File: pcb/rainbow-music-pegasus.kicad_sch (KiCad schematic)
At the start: 113 parts, among them J1 USB_B_Micro, J2 Conn_02x03_Odd_Even, J3 B2B-PH-K-S, Q1 DMG3415U, SW1 SW_SPDT, SW2 EVQQ2, U1 ESP32-C3-MINI-1, U2 OPA2322, U3 TLV75533PDBV, U4 MCP73831-2-OT, U5 MCP41050

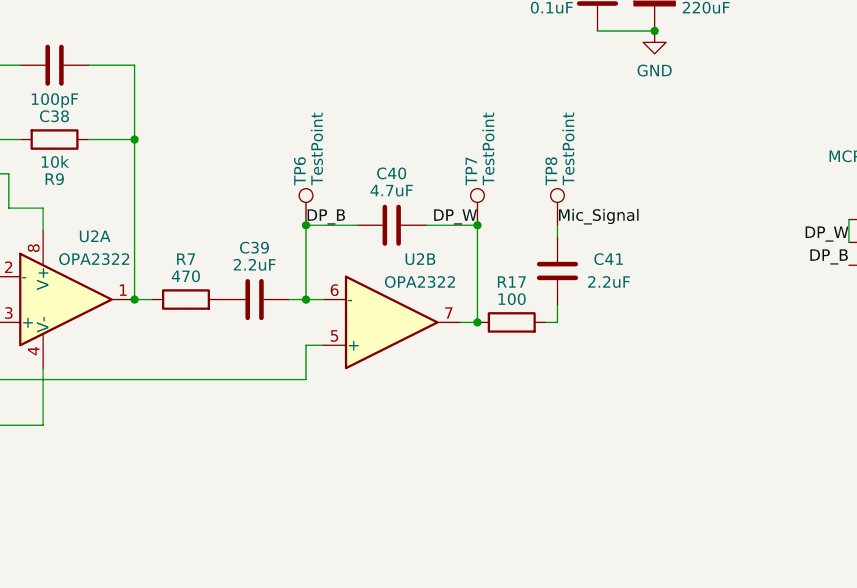
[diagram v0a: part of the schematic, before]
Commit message: Minor changes to the PCB and BOM to better support the digipot and signal
* Remove C40 (which was shunting the MCP41050 PB0 & PB0, reducing effectiveness)
* Raise R7 from 470 to 2.2k
* Raise R17 from 100 to 330
* Change C41 to a 0.1uF shunt cap to GND placed close to GPIO4

The R7 is raised 2.2k so the digipot wiper current stays within its +/-1
mA rating even if the first stage swings rail to rail, and so loud music
sits mid-range on the wiper where steps are finer (maximum stage-2 gain
is now ~23). With C39 (2.2uF) this also lowers the high-pass corner from
~154 Hz to ~33 Hz, letting bass through.

The ADC now sees U2B's 1.65 V output directly, as the firmware expects,
and R17/C41 form a ~4.8 kHz anti-aliasing filter and a charge reservoir
for ADC sampling.
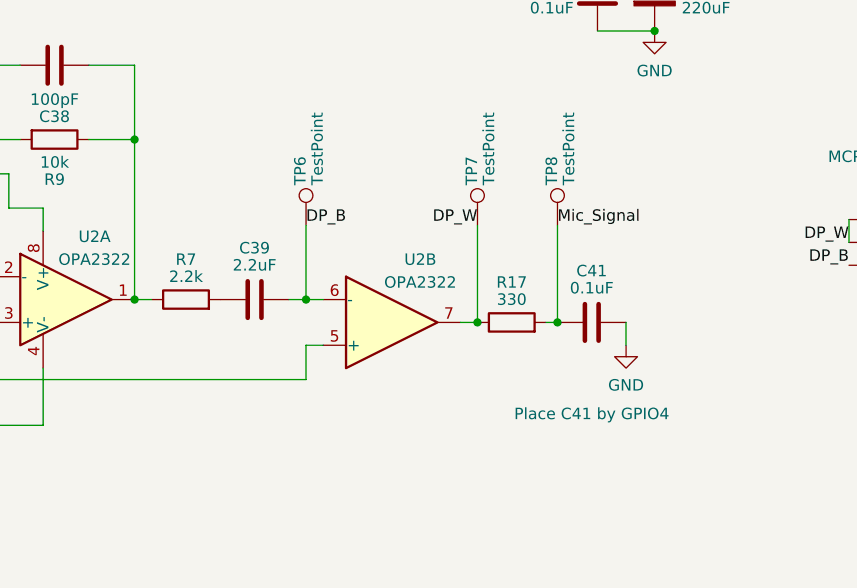
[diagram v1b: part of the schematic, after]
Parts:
- removed C40: 4.7uF, Capacitor_SMD:C_0805_2012Metric, symbol Device:C
- C41: value 2.2uF -> 0.1uF; footprint Capacitor_SMD:C_0805_2012Metric -> Capacitor_SMD:C_0603_1608Metric
- R17: value 100 -> 330
- R7: value 470 -> 2.2k; footprint Resistor_SMD:R_0603_1608Metric -> Resistor_SMD:R_0805_2012Metric
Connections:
- net GND: now also C41.2
- net Mic_Signal: now also R17.2
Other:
- moved on the sheet: C41
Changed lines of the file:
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@@
 	)
 	(junction
+		(at 142.24 73.025)
+		(diameter 0)
+		(color 0 0 0 0)
+	)
+	(junction
 		(at 366.395 238.125)
 		(diameter 0)
@@
 	)
 	(junction
-		(at 133.35 62.23)
-		(diameter 0)
-		(color 0 0 0 0)
-	)
-	(junction
 		(at 170.18 163.195)
 		(diameter 0)
@@
 	)
 	(junction
-		(at 114.3 62.23)
-		(diameter 0)
-		(color 0 0 0 0)
-	)
-	(junction
 		(at 281.305 39.37)
 		(diameter 0)
@@
 	(wire
 		(pts
-			(xy 114.3 62.23) (xy 120.015 62.23)
-		)
-		(stroke
-			(width 0)
-			(type default)
-		)
-	)
-	(wire
-		(pts
 			(xy 139.7 255.27) (xy 139.7 264.16)
 		)
@@
 	(wire
 		(pts
-			(xy 142.24 62.23) (xy 142.24 63.5)
+			(xy 142.24 62.23) (xy 142.24 73.025)
 		)
 		(stroke
@@
 	(wire
 		(pts
-			(xy 127.635 62.23) (xy 133.35 62.23)
-		)
-		(stroke
-			(width 0)
-			(type default)
-		)
-	)
-	(wire
-		(pts
 			(xy 114.3 79.375) (xy 114.3 75.565)
 		)
@@
 	(wire
 		(pts
-			(xy 85.09 60.325) (xy 85.09 62.865)
+			(xy 149.86 73.025) (xy 149.86 75.565)
 		)
 		(stroke
@@
 	(wire
 		(pts
-			(xy 340.995 231.775) (xy 340.995 230.505)
+			(xy 85.09 60.325) (xy 85.09 62.865)
 		)
 		(stroke
@@
 	(wire
 		(pts
-			(xy 334.645 221.615) (xy 334.645 220.345)
+			(xy 340.995 231.775) (xy 340.995 230.505)
 		)
 		(stroke
@@
 	(wire
 		(pts
-			(xy 372.745 220.345) (xy 379.095 220.345)
+			(xy 334.645 221.615) (xy 334.645 220.345)
 		)
 		(stroke
@@
 	(wire
 		(pts
-			(xy 175.895 232.41) (xy 185.42 232.41)
+			(xy 372.745 220.345) (xy 379.095 220.345)
 		)
 		(stroke
@@
 	(wire
 		(pts
-			(xy 218.44 161.925) (xy 220.345 161.925)
+			(xy 175.895 232.41) (xy 185.42 232.41)
 		)
 		(stroke
@@
 	(wire
 		(pts
-			(xy 142.24 73.025) (xy 142.24 71.12)
+			(xy 218.44 161.925) (xy 220.345 161.925)
 		)
 		(stroke
@@
 	(symbol
 		(lib_id "power:GND")
+		(at 149.86 75.565 0)
+		(mirror y)
+		(unit 1)
+		(body_style 1)
+		(exclude_from_sim no)
+		(in_bom yes)
+		(on_board yes)
+		(in_pos_files yes)
+		(dnp no)
+		(fields_autoplaced yes)
+		(property "Reference" "#PWR061"
+			(at 149.86 81.915 0)
+			(hide yes)
+			(show_name no)
+			(do_not_autoplace no)
+			(effects
+				(font
+					(size 1.27 1.27)
+				)
+			)
+		)
+		(property "Value" "GND"
+			(at 149.86 80.01 0)
+			(show_name no)
+			(do_not_autoplace no)
+			(effects
+				(font
+					(size 1.27 1.27)
+				)
+			)
+		)
+		(property "Footprint" ""
+			(at 149.86 75.565 0)
+			(hide yes)
+			(show_name no)
+			(do_not_autoplace no)
+			(effects
+				(font
+					(size 1.27 1.27)
+				)
+			)
+		)
+		(property "Datasheet" ""
+			(at 149.86 75.565 0)
+			(hide yes)
+			(show_name no)
+			(do_not_autoplace no)
+			(effects
+				(font
+					(size 1.27 1.27)
+				)
+			)
+		)
+		(property "Description" ""
+			(at 149.86 75.565 0)
+			(show_name no)
+			(do_not_autoplace no)
+			(effects
+				(font
+					(size 1.27 1.27)
+				)
+			)
+		)
+		(pin "1"
+		)
+		(instances
+			(project "rainbow-music-pegasus"
+				(path "/4cbaa20b-39f5-487e-a5d4-6b04539cf52b"
+					(reference "#PWR061")
+					(unit 1)
+				)
+			)
+		)
+	)
+	(symbol
+		(lib_id "power:GND")
 		(at 48.895 167.005 0)
 		(unit 1)
@@
 			)
 		)
-		(property "Value" "470"
+		(property "Value" "2.2k"
 			(at 100.965 67.945 90)
 			(show_name no)
@@
 			)
 		)
-		(property "Footprint" "Resistor_SMD:R_0603_1608Metric"
+		(property "Footprint" "Resistor_SMD:R_0805_2012Metric"
 			(at 100.965 72.263 90)
 			(hide yes)
@@
 			)
 		)
-		(property "Value" "100"
+		(property "Value" "330"
 			(at 137.16 70.485 90)
 			(show_name no)
@@
 	)
 	(symbol
-		(lib_id "Device:C")
-		(at 123.825 62.23 90)
-		(unit 1)
-		(body_style 1)
-		(exclude_from_sim no)
-		(in_bom yes)
-		(on_board yes)
-		(in_pos_files yes)
-		(dnp no)
-		(property "Reference" "C40"
-			(at 123.825 56.515 90)
-			(show_name no)
-			(do_not_autoplace no)
-			(effects
-				(font
-					(size 1.27 1.27)
-				)
-			)
-		)
-		(property "Value" "4.7uF"
-			(at 123.825 58.42 90)
-			(show_name no)
-			(do_not_autoplace no)
-			(effects
-				(font
-					(size 1.27 1.27)
-				)
-			)
-		)
-		(property "Footprint" "Capacitor_SMD:C_0805_2012Metric"
-			(at 127.635 61.2648 0)
-			(hide yes)
-			(show_name no)
-			(do_not_autoplace no)
-			(effects
-				(font
-					(size 1.27 1.27)
-				)
-			)
-		)
-		(property "Datasheet" ""
-			(at 123.825 62.23 0)
-			(hide yes)
-			(show_name no)
-			(do_not_autoplace no)
-			(effects
-				(font
-					(size 1.27 1.27)
-				)
-			)
-		)
-		(property "Description" ""
-			(at 123.825 62.23 0)
-			(show_name no)
-			(do_not_autoplace no)
-			(effects
-				(font
-					(size 1.27 1.27)
-				)
-			)
-		)
-		(pin "1"
-		)
-		(pin "2"
-		)
-		(instances
-			(project "rainbow-music-pegasus"
-				(path "/4cbaa20b-39f5-487e-a5d4-6b04539cf52b"
-					(reference "C40")
-					(unit 1)
-				)
-			)
-		)
-	)
-	(symbol
 		(lib_id "LED:WS2812B")
 		(at 147.32 240.03 270)
@@
 	(symbol
 		(lib_id "Device:C")
-		(at 142.24 67.31 0)
+		(at 146.05 73.025 90)
 		(unit 1)
 		(body_style 1)
@@
 		(dnp no)
 		(property "Reference" "C41"
-			(at 147.955 66.04 0)
+			(at 146.05 67.31 90)
 			(show_name no)
 			(do_not_autoplace no)
@@
 			)
 		)
-		(property "Value" "2.2uF"
-			(at 147.955 68.58 0)
+		(property "Value" "0.1uF"
+			(at 146.05 69.215 90)
 			(show_name no)
 			(do_not_autoplace no)
@@
 			)
 		)
-		(property "Footprint" "Capacitor_SMD:C_0805_2012Metric"
-			(at 143.2052 71.12 0)
+		(property "Footprint" "Capacitor_SMD:C_0603_1608Metric"
+			(at 149.86 72.0598 0)
 			(hide yes)
 			(show_name no)
@@
 		)
 		(property "Datasheet" ""
-			(at 142.24 67.31 0)
+			(at 146.05 73.025 0)
 			(hide yes)
 			(show_name no)
@@
 			)
 		)
-		(property "Description" ""
-			(at 142.24 67.31 0)
+		(property "Description" "Place C41 by GPIO4"
+			(at 146.05 83.185 90)
 			(show_name no)
 			(do_not_autoplace no)

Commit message: Move the button from GPIO9 to GPIO1
Eventually the button will be used as a factory reset (remove settings
like wifi configuration, etc) by holding down on power-on.  You cannot
do that with GPIO9 as that is already used to launch the bootloader on
power-on.

Actual button code and functionality still TBD.
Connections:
- net Boot: no longer C2.2, R2.2, SW2.1
- net Button: now reaches U1.13 (GPIO1/ADC1_CH1/XTAL_32K_N)
- net Button: now also C2.2, R2.2, SW2.1
- no-connect marks 6 -> 5
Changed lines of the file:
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@@
 	)
 	(no_connect
-		(at 268.605 57.15)
-	)
-	(no_connect
 		(at 261.62 262.89)
 	)
@@
 		)
 	)
+	(label "Button"
+		(at 368.3 80.01 0)
+		(effects
+			(font
+				(size 1.27 1.27)
+			)
+			(justify left bottom)
+		)
+	)
 	(label "Batt_Level"
 		(at 268.605 54.61 180)
@@
 		)
 	)
-	(label "Boot"
-		(at 368.3 80.01 0)
-		(effects
-			(font
-				(size 1.27 1.27)
-			)
-			(justify left bottom)
-		)
-	)
 	(label "RGB_Data"
 		(at 52.07 222.885 180)
@@
 		)
 	)
+	(label "Button"
+		(at 268.605 57.15 180)
+		(effects
+			(font
+				(size 1.27 1.27)
+			)
+			(justify right bottom)
+		)
+	)

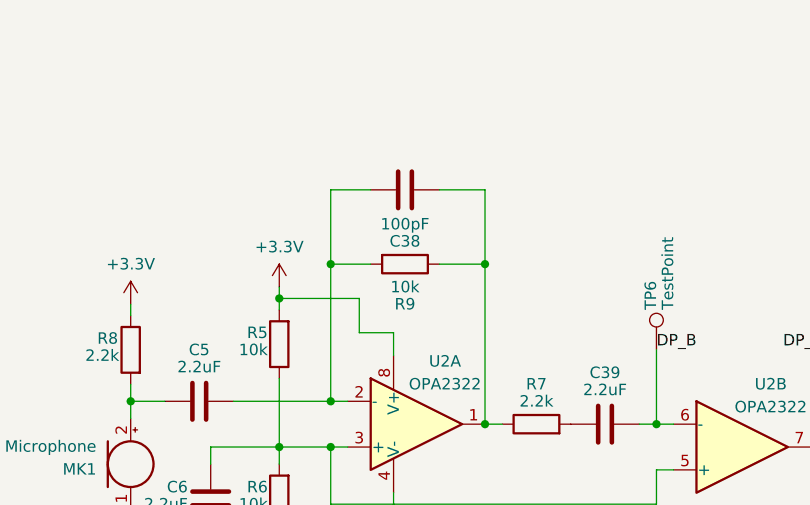
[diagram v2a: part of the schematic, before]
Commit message: Change C38 to a 1.5nF C0G
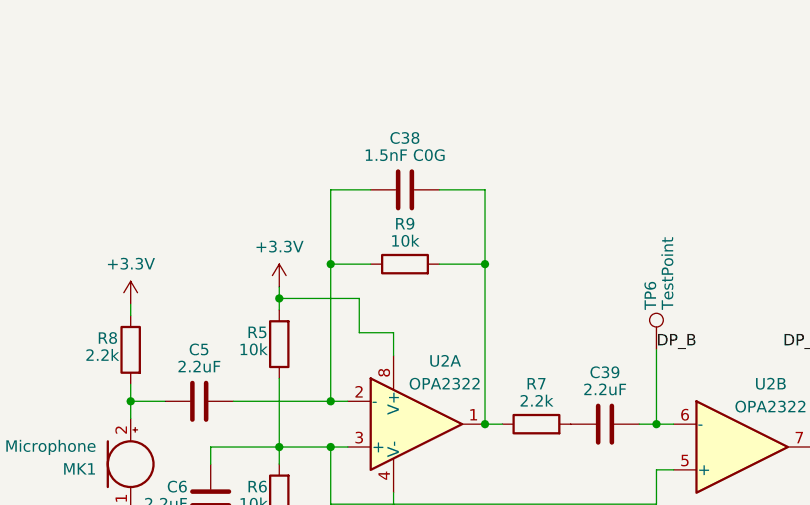
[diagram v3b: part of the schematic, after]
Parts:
- C38: value 100pF -> 1.5nF C0G
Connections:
- net at C38.1, R9.2: now also R7.1, U2.1; no longer C5.2, U2.2 (-)
- net at C38.2, R9.1: now also C5.2, U2.2 (-); no longer R7.1, U2.1
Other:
- moved on the sheet: C38, R9
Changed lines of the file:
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@@
 	(symbol
 		(lib_id "Device:C")
-		(at 86.36 44.45 90)
+		(at 86.36 44.45 270)
 		(mirror x)
 		(unit 1)
@@
 		(dnp no)
 		(property "Reference" "C38"
-			(at 86.36 50.165 90)
-			(show_name no)
-			(do_not_autoplace no)
-			(effects
-				(font
-					(size 1.27 1.27)
-				)
-			)
-		)
-		(property "Value" "100pF"
-			(at 86.36 48.26 90)
+			(at 86.36 38.735 90)
+			(show_name no)
+			(do_not_autoplace no)
+			(effects
+				(font
+					(size 1.27 1.27)
+				)
+			)
+		)
+		(property "Value" "1.5nF C0G"
+			(at 86.36 40.64 90)
 			(show_name no)
 			(do_not_autoplace no)
@@
 		)
 		(property "Footprint" "Capacitor_SMD:C_0805_2012Metric"
-			(at 90.17 45.4152 0)
+			(at 82.55 43.4848 0)
 			(hide yes)
 			(show_name no)
@@
 	(symbol
 		(lib_id "Device:R")
-		(at 86.36 52.705 270)
+		(at 86.36 52.705 90)
 		(unit 1)
 		(body_style 1)
@@
 		(dnp no)
 		(property "Reference" "R9"
-			(at 86.36 57.15 90)
+			(at 86.36 48.26 90)
 			(show_name no)
 			(do_not_autoplace no)
@@
 		)
 		(property "Value" "10k"
-			(at 86.36 55.245 90)
+			(at 86.36 50.165 90)
 			(show_name no)
 			(do_not_autoplace no)
@@
 		)
 		(property "Footprint" "Resistor_SMD:R_0805_2012Metric"
-			(at 86.36 50.927 90)
-			(hide yes)
-			(show_name no)
+			(at 86.36 54.483 90)
+			(hide yes)
+			(show_name no)
